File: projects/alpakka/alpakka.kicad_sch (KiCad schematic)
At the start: 76 parts, among them P1 Debug, P2 Endpoint, P3 Conn_01x02, Q1 Q_PMOS_DGS, U1 Raspberry_Pico, U10 ST_LSM6, U12 ST_LSM6, U2 Alpsalpine_RKJXV, U3 Alpsalpine_EC10E, U4 Alpsalpine_RKJXM, U6 NXP_PCAL6416A, U8 NXP_PCAL6416A

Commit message: fill some order info to BOM, also add 3d models of some parts
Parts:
- S1, S10, S11, S12, S14, S2, S3, S4, S5, S6, S7, S8, S9: digikey# (none) -> 4809-SKPMAME010CT-ND; manf (none) -> Alps Alpine; manf# (none) -> SKPMAME010
- S15, S16: digikey# (none) -> 4809-SKHHLNA010-ND; manf (none) -> Alps Alpine; manf# (none) -> SKHHLNA010
- S17, S18, S19, S20: digikey# (none) -> 4809-SKQGAFE010CT-ND; manf (none) -> Alps Alpine; manf# (none) -> SKQGAFE010
- U1: digikey# (none) -> 2648-SC1631CT-ND; manf (none) -> Raspberry Pi; manf# (none) -> SC1631
- U6, U8: value NXP_PCAL6416A -> PCAL6416A; digikey# (none) -> 568-9946-1-ND; manf (none) -> NXP USA Inc.; manf# (none) -> PCAL6416AHF,128

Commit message: add joystick 3d model and order info
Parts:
- U10: digikey# (none) -> 497-19479-1-ND; manf (none) -> STMicroelectronics; manf# (none) -> LSM6DSRTR
- U2: manf (none) -> Alps Alpine; manf# (none) -> RKJXV122400R; mouser# (none) -> 688-RKJXV122400R
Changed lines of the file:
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@@
 			)
 		)
-		(property "Description" ""
+		(property "Description" "Multi-Directional Switches 23degree max, 10Kohm 50V AC, 5V DC"
 			(at 90.17 77.47 0)
 			(effects
@@
 		)
 		(property "Export" ""
+			(at 90.17 77.47 0)
+			(effects
+				(font
+					(size 1.27 1.27)
+				)
+				(hide yes)
+			)
+		)
+		(property "manf" "Alps Alpine"
+			(at 90.17 77.47 0)
+			(effects
+				(font
+					(size 1.27 1.27)
+				)
+				(hide yes)
+			)
+		)
+		(property "manf#" "RKJXV122400R"
+			(at 90.17 77.47 0)
+			(effects
+				(font
+					(size 1.27 1.27)
+				)
+				(hide yes)
+			)
+		)
+		(property "digikey#" ""
+			(at 90.17 77.47 0)
+			(effects
+				(font
+					(size 1.27 1.27)
+				)
+				(hide yes)
+			)
+		)
+		(property "mouser#" "688-RKJXV122400R"
 			(at 90.17 77.47 0)
 			(effects
@@
 			)
 		)
-		(property "Description" ""
+		(property "Description" "Accelerometer, Gyroscope, Temperature, 6 Axis Sensor I2C, SPI Output"
 			(at 95.25 124.46 0)
 			(effects
@@
 			(at 95.25 124.46 0)
 			(effects
+				(font
+					(size 1.27 1.27)
+				)
+				(hide yes)
+			)
+		)
+		(property "manf" "STMicroelectronics"
+			(at 95.25 124.46 0)
+			(effects
+				(font
+					(size 1.27 1.27)
+				)
+				(hide yes)
+			)
+		)
+		(property "manf#" "LSM6DSRTR"
+			(at 95.25 124.46 0)
+			(effects
+				(font
+					(size 1.27 1.27)
+				)
+				(hide yes)
+			)
+		)
+		(property "digikey#" "497-19479-1-ND"
+			(at 95.25 124.46 0)
+			(effects

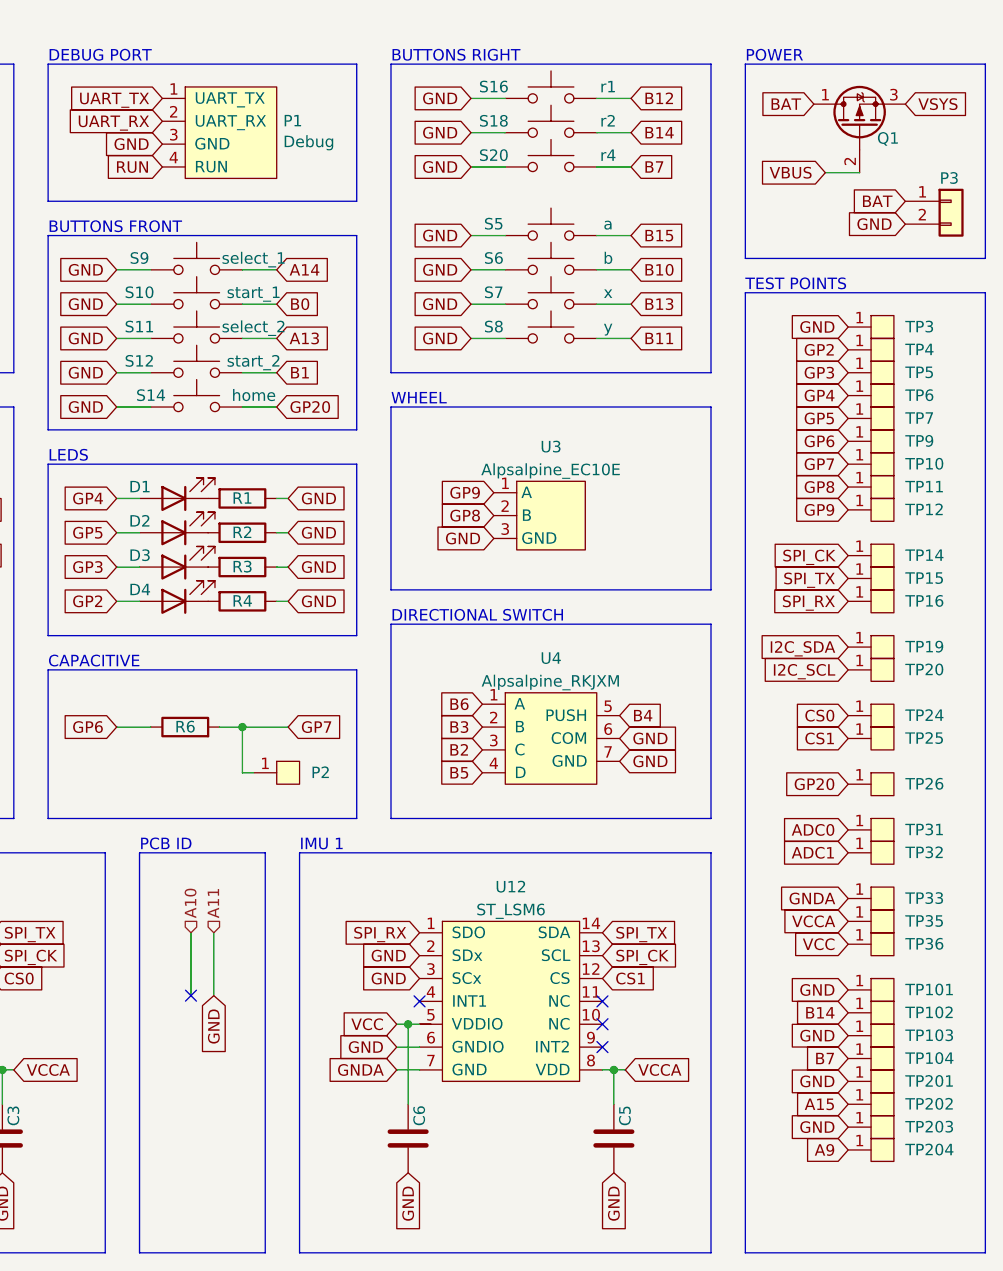
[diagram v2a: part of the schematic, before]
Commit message: add info + 3d model for the right joystick
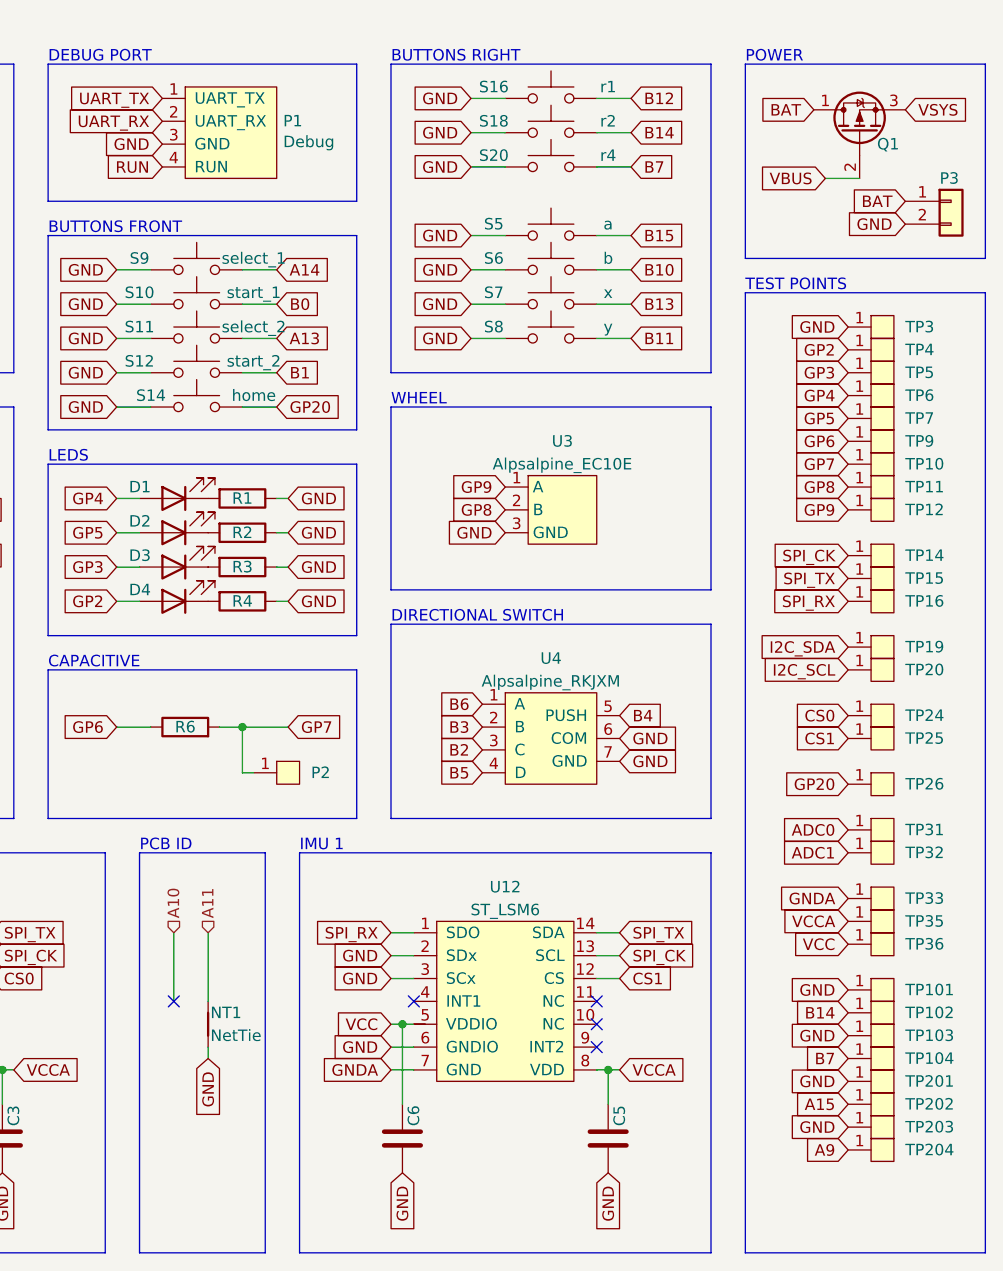
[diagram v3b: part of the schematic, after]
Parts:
- added NT1: NetTie, symbol Device:NetTie_2
- U4: digikey# (none) -> 4809-RKJXM1015004-ND; manf (none) -> Alps Alpine; manf# (none) -> RKJXM1015004
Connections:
- net GND: now also NT1.1; no longer U6.13 (P11)
- new net A11: NT1.2, U6.13 (P11)
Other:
- moved on the sheet: C5, C6, Q1, U12, U3

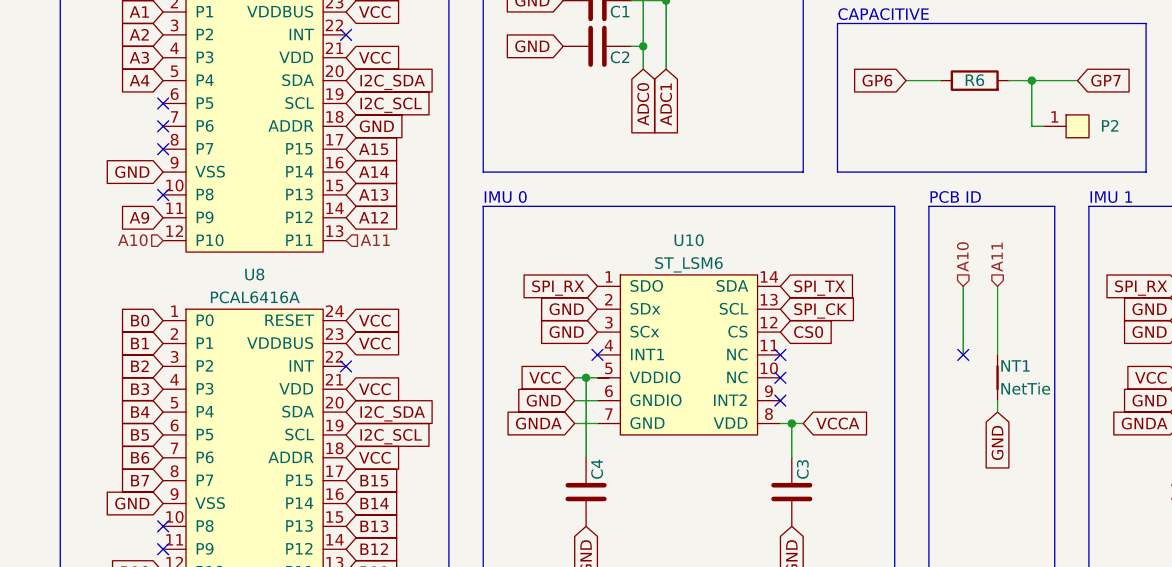
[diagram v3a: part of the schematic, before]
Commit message: replace capacitive contact part with one with 3d model
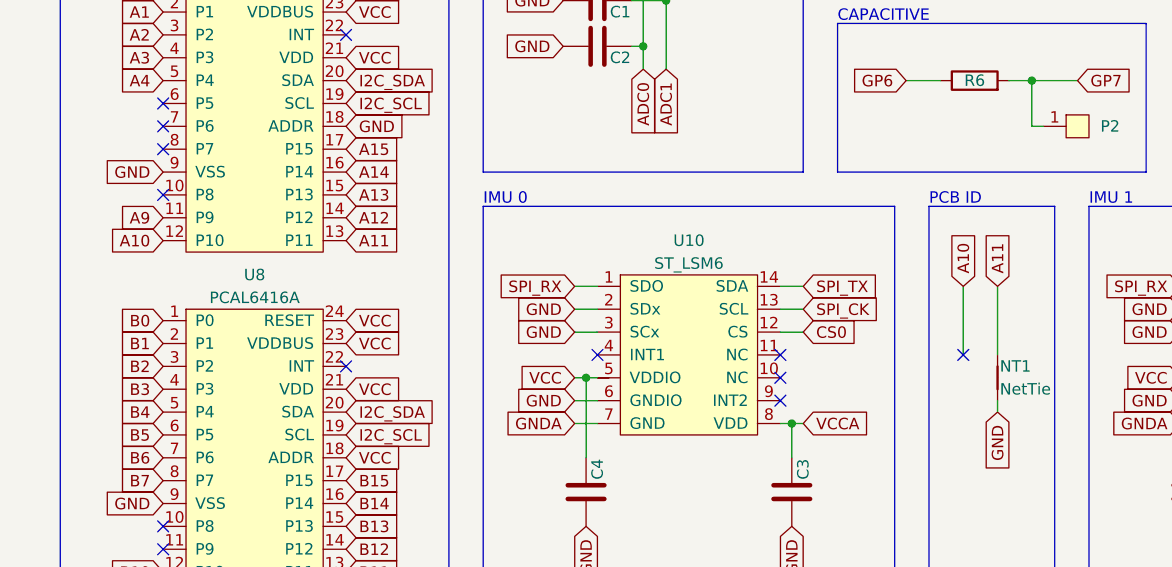
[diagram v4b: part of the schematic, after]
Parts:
- P2: footprint ILO_fp:HRO_BC-25-3P -> ILO_fp:304D-262503; digikey# (none) -> 4827-304D-262503CT-ND; manf (none) -> ATTEND Technology; manf# (none) -> 304D-262503
- U12: digikey# (none) -> 497-19479-1-ND; manf (none) -> STMicroelectronics; manf# (none) -> LSM6DSRTR
- U3: digikey# (none) -> 4809-EC10E1220503-ND; manf (none) -> Alps Alpine; manf# (none) -> EC10E1220503
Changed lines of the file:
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@@
 	(wire
 		(pts
+			(xy 82.55 123.19) (xy 85.09 123.19)
+		)
+		(stroke
+			(width 0)
+			(type default)
+		)
+	)
+	(wire
+		(pts
 			(xy 82.55 133.35) (xy 85.09 133.35)
 		)
@@
 		)
 	)
+	(wire
+		(pts
+			(xy 107.95 120.65) (xy 105.41 120.65)
+		)
+		(stroke
+			(width 0)
+			(type default)
+		)
+	)
 	(polyline
 		(pts
@@
 	(wire
 		(pts
+			(xy 107.95 123.19) (xy 105.41 123.19)
+		)
+		(stroke
+			(width 0)
+			(type default)
+		)
+	)
+	(wire
+		(pts
 			(xy 133.35 102.87) (xy 134.62 102.87)
 		)
@@
 	(wire
 		(pts
+			(xy 107.95 125.73) (xy 105.41 125.73)
+		)
+		(stroke
+			(width 0)
+			(type default)
+		)
+	)
+	(wire
+		(pts
 			(xy 105.41 135.89) (xy 106.68 135.89)
 		)
@@
 	(wire
 		(pts
+			(xy 82.55 120.65) (xy 85.09 120.65)
+		)
+		(stroke
+			(width 0)
+			(type default)
+		)
+	)
+	(wire
+		(pts
 			(xy 119.38 97.79) (xy 123.19 97.79)
 		)
@@
 		)
 	)
+	(wire
+		(pts
+			(xy 82.55 125.73) (xy 85.09 125.73)
+		)
+		(stroke
+			(width 0)
+			(type default)
+		)
+	)
 	(polyline
 		(pts
@@
 		)
 	)
+	(global_label "A11"
+		(shape input)
+		(at 129.54 120.65 90)
+		(fields_autoplaced yes)
+		(effects
+			(font
+				(size 1.27 1.27)
+			)
+			(justify left)
+		)
+		(property "Intersheetrefs" "${INTERSHEET_REFS}"
+			(at 129.54 114.1572 90)
+			(effects
+				(font
+					(size 1.27 1.27)
+				)
+				(justify left)
+				(hide yes)
+			)
+		)
+	)
+	(global_label "A10"
+		(shape input)
+		(at 36.83 115.57 180)
+		(fields_autoplaced yes)
+		(effects
+			(font
+				(size 1.27 1.27)
+			)
+			(justify right)
+		)
+		(property "Intersheetrefs" "${INTERSHEET_REFS}"
+			(at 30.3372 115.57 0)
+			(effects
+				(font
+					(size 1.27 1.27)
+				)
+				(justify right)
+				(hide yes)
+			)
+		)
+	)
 	(global_label "SPI_CK"
 		(shape input)
-		(at 105.41 123.19 0)
+		(at 107.95 123.19 0)
 		(fields_autoplaced yes)
 		(effects
@@
 		)
 		(property "Intersheetrefs" "${INTERSHEET_REFS}"
-			(at 114.3261 123.1106 0)
+			(at 116.8661 123.1106 0)
 			(effects
 				(font
@@
 		)
 	)
+	(global_label "A11"
+		(shape input)
+		(at 57.15 115.57 0)
+		(fields_autoplaced yes)
+		(effects
+			(font
+				(size 1.27 1.27)
+			)
+			(justify left)
+		)
+		(property "Intersheetrefs" "${INTERSHEET_REFS}"
+			(at 63.6428 115.57 0)
+			(effects
+				(font
+					(size 1.27 1.27)
+				)
+				(justify left)
+				(hide yes)
+			)
+		)
+	)
 	(global_label "VCC"
 		(shape input)
@@
 	(global_label "SPI_RX"
 		(shape input)
-		(at 85.09 120.65 180)
+		(at 82.55 120.65 180)
 		(fields_autoplaced yes)
 		(effects
@@
 		)
 		(property "Intersheetrefs" "${INTERSHEET_REFS}"
-			(at 76.2344 120.5706 0)
+			(at 73.6944 120.5706 0)
 			(effects
 				(font
@@
 	(global_label "GND"
 		(shape input)
-		(at 85.09 123.19 180)
+		(at 82.55 123.19 180)
 		(fields_autoplaced yes)
 		(effects
@@
 		)
 		(property "Intersheetrefs" "${INTERSHEET_REFS}"
-			(at 78.8953 123.1106 0)
+			(at 76.3553 123.1106 0)
 			(effects
 				(font
@@
 	(global_label "CS0"
 		(shape input)
-		(at 105.41 125.73 0)
+		(at 107.95 125.73 0)
 		(fields_autoplaced yes)
 		(effects
@@
 		)
 		(property "Intersheetrefs" "${INTERSHEET_REFS}"
-			(at 111.4232 125.6506 0)
+			(at 113.9632 125.6506 0)
 			(effects
 				(font
@@
 	(global_label "SPI_TX"
 		(shape input)
-		(at 105.41 120.65 0)
+		(at 107.95 120.65 0)
 		(fields_autoplaced yes)
 		(effects
@@
 		)
 		(property "Intersheetrefs" "${INTERSHEET_REFS}"
-			(at 113.9632 120.5706 0)
+			(at 116.5032 120.5706 0)
 			(effects
 				(font
@@
 		)
 	)
+	(global_label "A10"
+		(shape input)
+		(at 125.73 120.65 90)
+		(fields_autoplaced yes)
+		(effects
+			(font
+				(size 1.27 1.27)
+			)
+			(justify left)
+		)
+		(property "Intersheetrefs" "${INTERSHEET_REFS}"
+			(at 125.73 114.1572 90)
+			(effects
+				(font
+					(size 1.27 1.27)
+				)
+				(justify left)
+				(hide yes)
+			)
+		)
+	)
 	(global_label "GND"
 		(shape input)
@@
 	(global_label "GND"
 		(shape input)
-		(at 85.09 125.73 180)
+		(at 82.55 125.73 180)
 		(fields_autoplaced yes)
 		(effects
@@
 		)
 		(property "Intersheetrefs" "${INTERSHEET_REFS}"
-			(at 78.8953 125.6506 0)
+			(at 76.3553 125.6506 0)
 			(effects
 				(font
@@
 		)
 	)
-	(hierarchical_label "A11"
-		(shape input)
-		(at 129.54 120.65 90)
-		(fields_autoplaced yes)
-		(effects
-			(font
-				(size 1.27 1.27)
-			)
-			(justify left)
-		)
-	)
-	(hierarchical_label "A11"
-		(shape input)
-		(at 57.15 115.57 0)
-		(fields_autoplaced yes)
-		(effects
-			(font
-				(size 1.27 1.27)
-			)
-			(justify left)
-		)
-	)
-	(hierarchical_label "A10"
-		(shape input)
-		(at 36.83 115.57 180)
-		(fields_autoplaced yes)
-		(effects
-			(font
-				(size 1.27 1.27)
-			)
-			(justify right)
-		)
-	)
-	(hierarchical_label "A10"
-		(shape input)
-		(at 125.73 120.65 90)
-		(fields_autoplaced yes)
-		(effects
-			(font
-				(size 1.27 1.27)
-			)
-			(justify left)
-		)
-	)
 	(symbol
 		(lib_id "ILO_sym:Raspberry_Pico")
@@
 			)
 		)
-		(property "Footprint" "ILO_fp:HRO_BC-25-3P"
+		(property "Footprint" "ILO_fp:304D-262503"
 			(at 138.43 102.87 0)
 			(effects
@@
 			)
 		)
-		(property "Datasheet" ""
+		(property "Datasheet" "https://www.attend.com.tw/data/download/file/304D-2625XX_B_2.pdf"
 			(at 138.43 102.87 0)
 			(effects
@@
 			)
 		)
-		(property "Description" ""
+		(property "Description" "3 Position Spring Battery Contact Connector Surface Mount"
 			(at 138.43 102.87 0)
 			(effects
@@
 			)
 		)
+		(property "manf" "ATTEND Technology"
+			(at 138.43 102.87 0)
+			(effects
+				(font
+					(size 1.27 1.27)
+				)
+				(hide yes)
+			)
+		)
+		(property "manf#" "304D-262503"
+			(at 138.43 102.87 0)
+			(effects
+				(font
+					(size 1.27 1.27)
+				)
+				(hide yes)
+			)
+		)
+		(property "digikey#" "4827-304D-262503CT-ND"
+			(at 138.43 102.87 0)
+			(effects
+				(font
+					(size 1.27 1.27)
+				)
+				(hide yes)
+			)
+		)
 		(pin "1"
 		)
@@
 			)
 		)
-		(property "Datasheet" ""
+		(property "Datasheet" "https://www.st.com/resource/en/datasheet/lsm6dsr.pdf"
 			(at 162.56 113.03 0)
 			(effects
@@
 			)
 		)
-		(property "Description" ""
+		(property "Description" "Accelerometer, Gyroscope, Temperature, 6 Axis Sensor I2C, SPI Output"
 			(at 162.56 124.46 0)
 			(effects
@@
 			)
 		)
+		(property "digikey#" "497-19479-1-ND"
+			(at 162.56 124.46 0)
+			(effects
+				(font
+					(size 1.27 1.27)
+				)
+				(hide yes)
+			)
+		)
+		(property "manf" "STMicroelectronics"
+			(at 162.56 124.46 0)
+			(effects
+				(font
+					(size 1.27 1.27)
+				)
+				(hide yes)
+			)
+		)
+		(property "manf#" "LSM6DSRTR"
+			(at 162.56 124.46 0)
+			(effects
+				(font
+					(size 1.27 1.27)
+				)
+				(hide yes)
+			)
+		)
 		(pin "1"
 		)
@@
 			)
 		)
-		(property "Datasheet" ""
+		(property "Datasheet" "https://www.st.com/resource/en/datasheet/lsm6dsr.pdf"
 			(at 95.25 113.03 0)
 			(effects
@@
 			)
 		)
-		(property "Datasheet" ""
+		(property "Datasheet" "https://tech.alpsalpine.com/e/products/detail/EC10E1220505/"
 			(at 168.91 72.39 0)
 			(effects
@@
 			)
 		)
-		(property "Description" ""
+		(property "Description" "Rotary Encoder Mechanical 12 Quadrature (Incremental) Vertical"
 			(at 168.91 73.66 0)
 			(effects
@@
 			(at 168.91 73.66 0)
 			(effects
+				(font
+					(size 1.27 1.27)
+				)
+				(hide yes)
+			)
+		)
+		(property "manf" "Alps Alpine"
+			(at 168.91 73.66 0)
+			(effects
+				(font
+					(size 1.27 1.27)
+				)
+				(hide yes)
+			)
+		)
+		(property "manf#" "EC10E1220503"
+			(at 168.91 73.66 0)
+			(effects
+				(font
+					(size 1.27 1.27)
+				)
+				(hide yes)
+			)
+		)
+		(property "digikey#" "4809-EC10E1220503-ND"
+			(at 168.91 73.66 0)
+			(effects

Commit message: add resistor order info
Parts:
- C1, C2, C3, C4, C5, C6: footprint ILO_fp:0402 -> Capacitor_SMD:C_0402_1005Metric_Pad0.74x0.62mm_HandSolder; digikey# (none) -> 1276-1001-1-ND; manf (none) -> Samsung Electro-Mechanics; manf# (none) -> CL05B104KO5NNNC
- NT1: footprint (none) -> NetTie:NetTie-2_SMD_Pad0.5mm
- R1, R2, R3, R4: footprint ILO_fp:0603 -> Resistor_SMD:R_0603_1608Metric_Pad0.98x0.95mm_HandSolder; digikey# (none) -> P20.0HCT-ND; manf (none) -> Panasonic Electronic Components; manf# (none) -> ERJ-3EKF20R0V
- R6: footprint ILO_fp:0402 -> Resistor_SMD:R_0402_1005Metric_Pad0.72x0.64mm_HandSolder; digikey# (none) -> P510KLCT-ND; manf (none) -> Panasonic Electronic Components; manf# (none) -> ERJ-2RKF5103X
